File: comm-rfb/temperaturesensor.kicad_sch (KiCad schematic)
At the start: 5 parts

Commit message: comm-rfb: reformat main schematic page
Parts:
- gave numbers to parts that had none: 5
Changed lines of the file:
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@@
   (symbol (lib_id "power:GND") (at 106.68 76.2 0) (unit 1)
     (in_bom yes) (on_board yes) (fields_autoplaced)
-    (property "Reference" "#PWR?" (id 0) (at 106.68 82.55 0)
+    (property "Reference" "#PWR020" (id 0) (at 106.68 82.55 0)
       (effects (font (size 1.27 1.27)) hide)
     )
@@
   (symbol (lib_id "Simulation_SPICE:DIODE") (at 146.812 95.25 270) (unit 1)
     (in_bom yes) (on_board yes)
-    (property "Reference" "D?" (id 0) (at 148.844 93.2179 90)
+    (property "Reference" "D3" (id 0) (at 148.844 93.2179 90)
       (effects (font (size 1.27 1.27)) (justify left))
     )
@@
   (symbol (lib_id "Daughterboard_Symbols:MCP9808T-E{brace}slash}MC") (at 106.68 68.58 0) (unit 1)
     (in_bom yes) (on_board yes) (fields_autoplaced)
-    (property "Reference" "U?" (id 0) (at 137.16 57.658 0)
+    (property "Reference" "U4" (id 0) (at 137.16 57.658 0)
       (effects (font (size 1.524 1.524)))
     )
@@
   (symbol (lib_id "power:GND") (at 146.812 108.966 0) (unit 1)
     (in_bom yes) (on_board yes) (fields_autoplaced)
-    (property "Reference" "#PWR?" (id 0) (at 146.812 115.316 0)
+    (property "Reference" "#PWR021" (id 0) (at 146.812 115.316 0)
       (effects (font (size 1.27 1.27)) hide)
     )
@@
   (symbol (lib_id "power:GND") (at 154.178 103.632 0) (unit 1)
     (in_bom yes) (on_board yes) (fields_autoplaced)
-    (property "Reference" "#PWR?" (id 0) (at 154.178 109.982 0)
+    (property "Reference" "#PWR022" (id 0) (at 154.178 109.982 0)
       (effects (font (size 1.27 1.27)) hide)
     )
@@
   (symbol (lib_id "power:GND") (at 169.418 76.2 90) (unit 1)
     (in_bom yes) (on_board yes) (fields_autoplaced)
-    (property "Reference" "#PWR?" (id 0) (at 175.768 76.2 0)
+    (property "Reference" "#PWR024" (id 0) (at 175.768 76.2 0)
       (effects (font (size 1.27 1.27)) hide)
     )
@@
   (symbol (lib_id "power:GND") (at 167.64 68.58 90) (unit 1)
     (in_bom yes) (on_board yes) (fields_autoplaced)
-    (property "Reference" "#PWR?" (id 0) (at 173.99 68.58 0)
+    (property "Reference" "#PWR023" (id 0) (at 173.99 68.58 0)
       (effects (font (size 1.27 1.27)) hide)
     )
@@
   (symbol (lib_id "Device:R") (at 146.812 103.632 0) (unit 1)
     (in_bom yes) (on_board yes)
-    (property "Reference" "R?" (id 0) (at 148.844 101.5999 0)
+    (property "Reference" "R9" (id 0) (at 148.844 101.5999 0)
       (effects (font (size 1.27 1.27)) (justify left))
     )
@@
   (symbol (lib_id "Device:FerriteBead_Small") (at 139.192 90.424 270) (unit 1)
     (in_bom yes) (on_board yes) (fields_autoplaced)
-    (property "Reference" "FB?" (id 0) (at 139.2301 84.074 90))
+    (property "Reference" "FB4" (id 0) (at 139.2301 84.074 90))
     (property "Value" "100R @ 100 MHz" (id 1) (at 139.2301 86.614 90))
     (property "Footprint" "Daughterboard_footprints:BEADC1608X75N" (id 2) (at 139.192 88.646 90)
@@
   (symbol (lib_id "Daughterboard_Symbols:CL10B104KB8NNNL") (at 154.178 93.98 270) (unit 1)
     (in_bom yes) (on_board yes)
-    (property "Reference" "C?" (id 0) (at 156.972 93.9799 90)
+    (property "Reference" "C11" (id 0) (at 156.972 93.9799 90)
       (effects (font (size 1.27 1.27)) (justify left))
     )

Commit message: comm-rfb: reduce number of sheets in schematic
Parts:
- removed FB4: 100R @ 100 MHz, Daughterboard_footprints:BEADC1608X75N, symbol Device:FerriteBead_Small
- removed U4: MCP9808T-E/MC, Daughterboard_footprints:SOP65P490X110-8N, symbol Daughterboard_Symbols:MCP9808T-E{brace}slash}MC
- added U4: MCP9808T-E/MC, qset-footprints:MCP9808T-E&slash_MC, symbol MCP9808T-EMC:MCP9808T-E/MC
- C11: footprint CAPC1608X90N -> Capacitor_SMD:C_0603_1608Metric
- D3: footprint Daughterboard_footprints:CAPC1608X90N -> Diode_SMD:D_0603_1608Metric
- R9: footprint Daughterboard_footprints:RESC1608X55N -> Resistor_SMD:R_0603_1608Metric
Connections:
- net GND: now also U4.4 (GND), U4.5 (A2), U4.6 (A1), U4.7 (A0), U4.9 (EPAD)
- net I2C2-SCLK: now also U4.2 (SCL)
- net I2C2-SDA: now also U4.1 (SDA)
- net TEMP-ALERT: now also U4.3 (ALERT)
- net +3V3: now reaches C11.1, D3.1 (A)
- net +3V3: now also U4.8 (VDD)
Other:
- moved on the sheet: C11, D3, R9

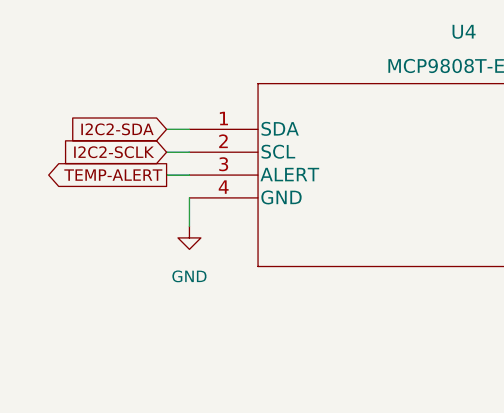
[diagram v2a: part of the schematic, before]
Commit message: comm-rfb: continue with new layout
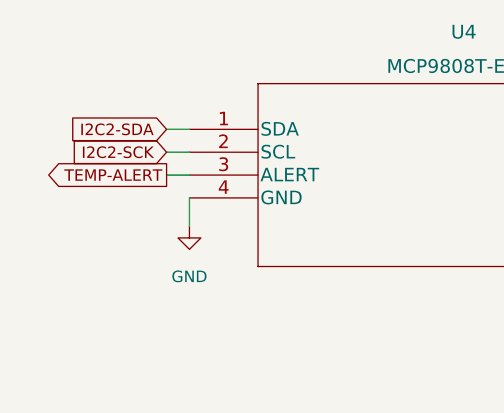
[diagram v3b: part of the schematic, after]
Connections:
- net I2C2-SCLK renamed I2C2-SCK
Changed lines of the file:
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@@
     )
   )
-  (global_label "I2C2-SCLK" (shape input) (at 104.14 71.12 180) (fields_autoplaced)
+  (global_label "I2C2-SCK" (shape input) (at 104.14 71.12 180) (fields_autoplaced)
     (effects (font (size 1.27 1.27)) (justify right))
-    (property "Intersheet References" "${INTERSHEET_REFS}" (id 0) (at 91.0831 71.0406 0)
+    (property "Intersheet References" "${INTERSHEET_REFS}" (id 0) (at 92.1112 71.0406 0)
       (effects (font (size 1.27 1.27)) (justify right) hide)
     )
